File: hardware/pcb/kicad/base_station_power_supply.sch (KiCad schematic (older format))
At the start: 19 parts, among them CON1 CONN_2, IC1 BRIDGE_TART, SW1 SWITCH

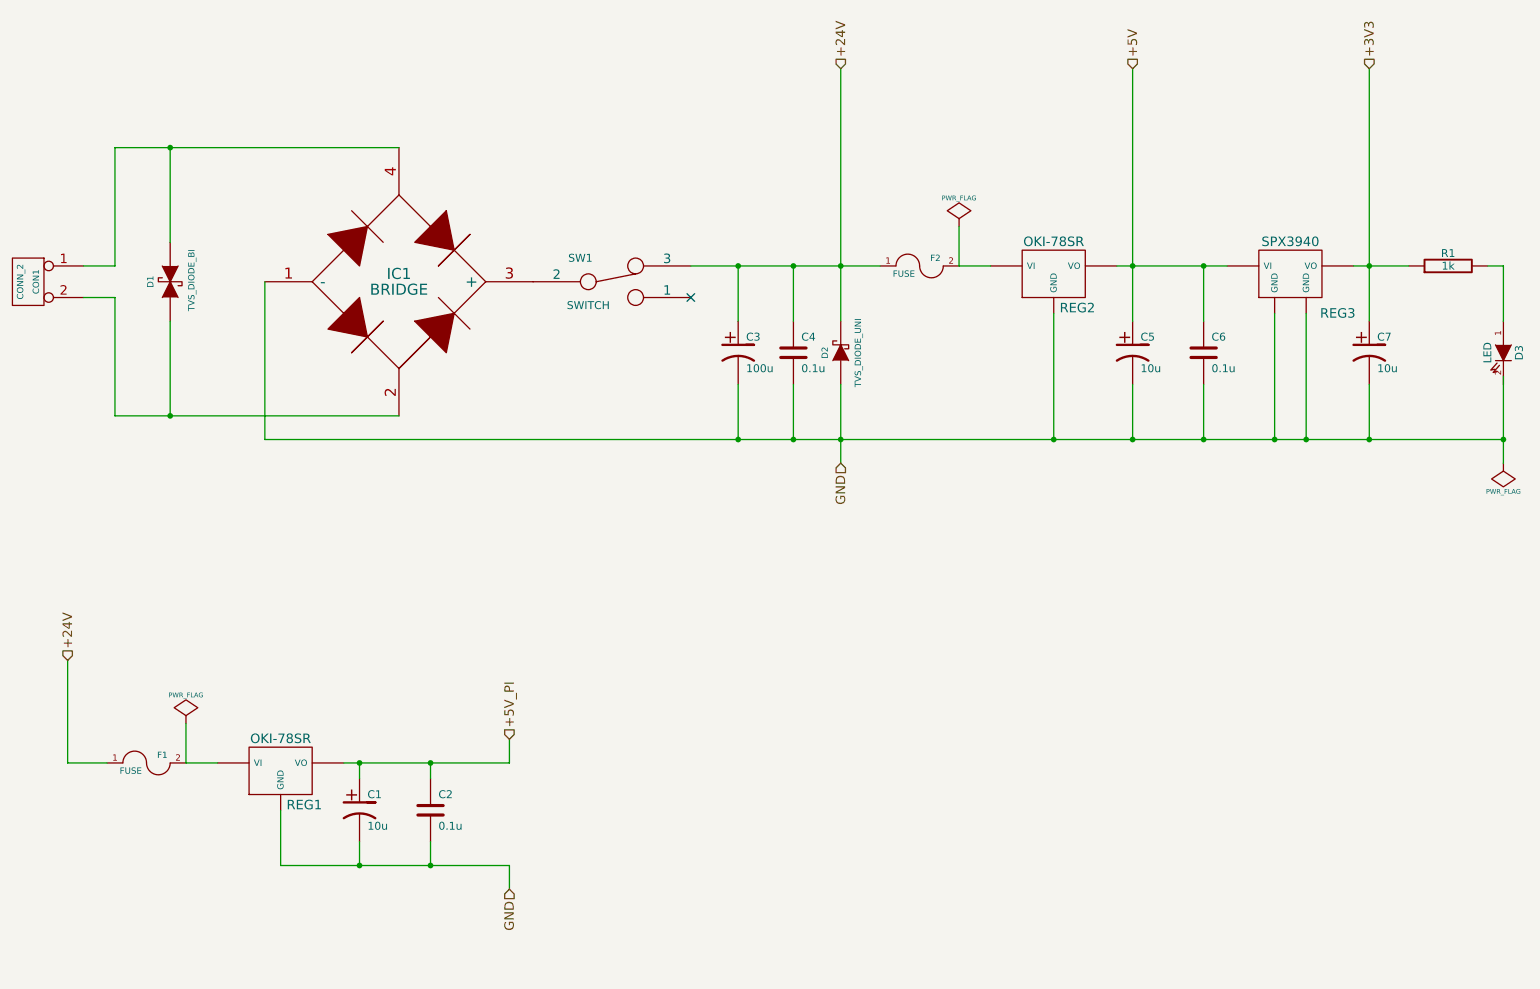
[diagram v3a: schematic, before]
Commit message: Made component references more logical - very similar to eagle version
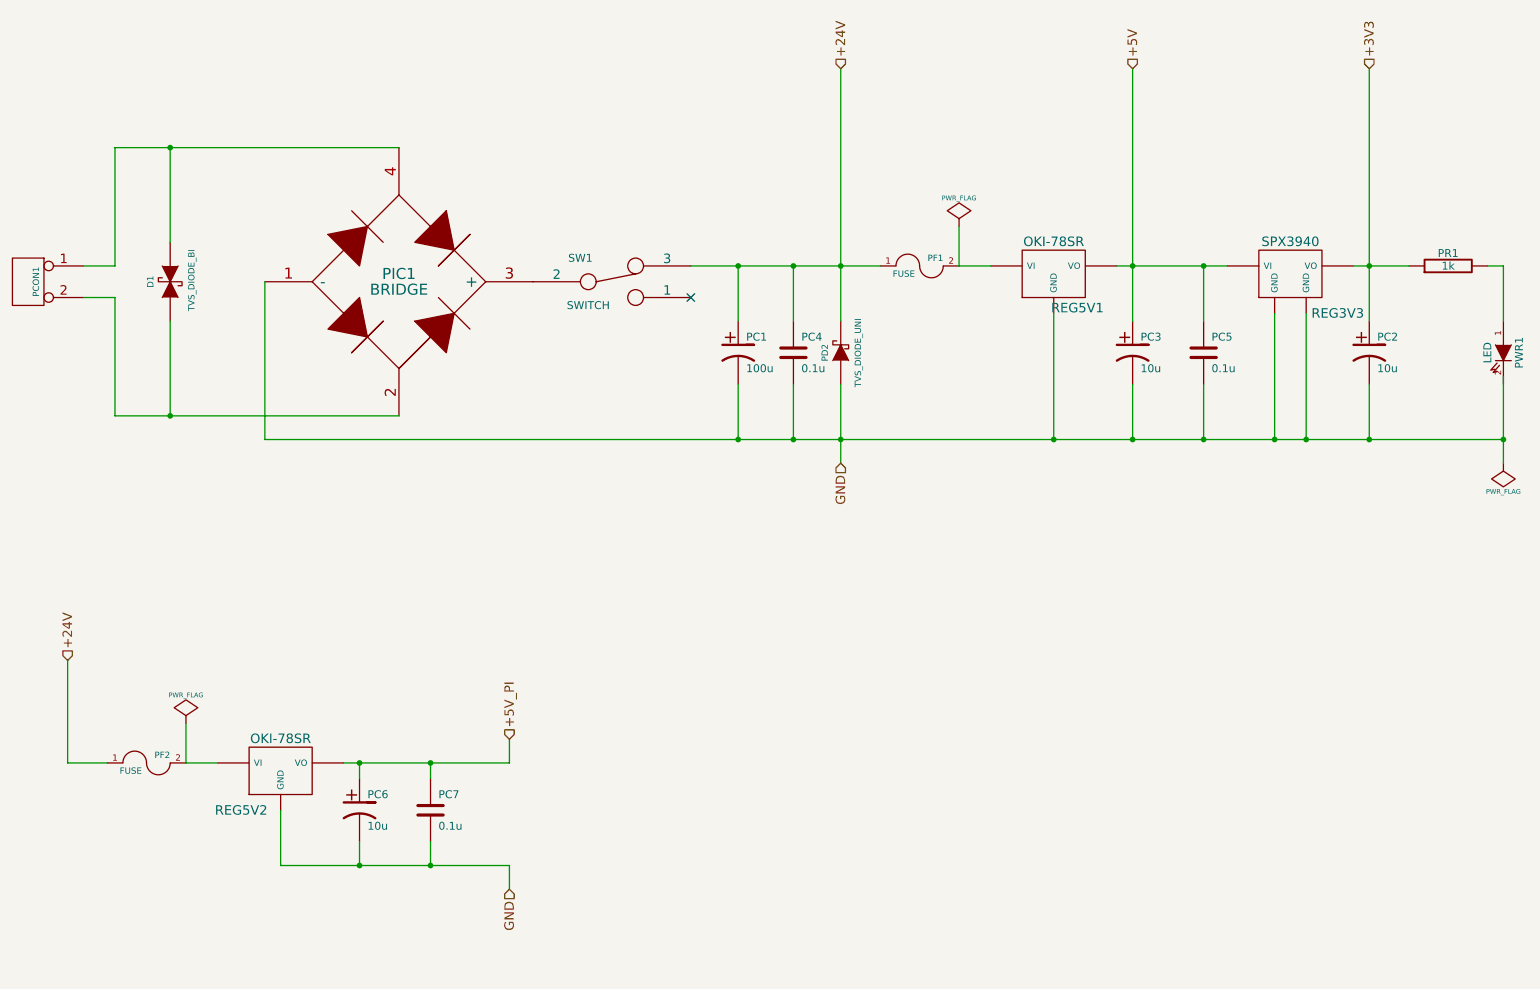
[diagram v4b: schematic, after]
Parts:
- PCON1: renamed from CON1; value CONN_2 -> ~
- renumbered C3 to PC1, C7 to PC2, C5 to PC3, C4 to PC4, C6 to PC5, C1 to PC6, C2 to PC7, D2 to PD2, F2 to PF1, F1 to PF2, IC1 to PIC1, R1 to PR1, D3 to PWR1, REG3 to REG3V3, REG2 to REG5V1, REG1 to REG5V2
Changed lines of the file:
@@
 Sheet 2 7
 Title ""
-Date "4 dec 2014"
+Date "8 dec 2014"
 Rev ""
 Comp ""
@@
 $EndDescr
 $Comp
-L FUSE F1
+L FUSE PF2
 U 1 1 5421F748
 P 1850 5500
-F 0 "F1" H 1950 5550 40  0000 C CNN
+F 0 "PF2" H 1950 5550 40  0000 C CNN
 F 1 "FUSE" H 1750 5450 40  0000 C CNN
 F 2 "" H 1850 5500 60  0001 C CNN
@@
 +5V_PI
 $Comp
-L CP1 C1
+L CP1 PC6
 U 1 1 5421F74A
 P 3200 5800
-F 0 "C1" H 3250 5900 50  0000 L CNN
+F 0 "PC6" H 3250 5900 50  0000 L CNN
 F 1 "10u" H 3250 5700 50  0000 L CNN
 F 2 "E5-10,5_TART" H 3200 5800 60  0001 C CNN
@@
 $EndComp
 $Comp
-L C C2
+L C PC7
 U 1 1 5421F749
 P 3650 5800
-F 0 "C2" H 3700 5900 50  0000 L CNN
+F 0 "PC7" H 3700 5900 50  0000 L CNN
 F 1 "0.1u" H 3700 5700 50  0000 L CNN
 F 2 "" H 3650 5800 60  0001 C CNN
@@
 $EndComp
 $Comp
-L OK1-78SR_TART REG1
+L OK1-78SR_TART REG5V2
 U 1 1 5421F746
 P 2700 5550
-F 0 "REG1" H 2850 5334 60  0000 C CNN
+F 0 "REG5V2" H 2450 5300 60  0000 C CNN
 F 1 "OK1-78SR_TART" H 2700 5860 60  0001 C CNN
 F 2 "" H 2700 5550 60  0001 C CNN
@@
 $EndComp
 $Comp
-L SPX3940_TART REG3
+L SPX3940_TART REG3V3
 U 1 1 5419032C
 P 9100 2400
-F 0 "REG3" H 9400 2150 60  0000 C CNN
+F 0 "REG3V3" H 9400 2150 60  0000 C CNN
 F 1 "SPX3940_TART" H 9100 2710 60  0001 C CNN
 F 2 "" H 9100 2400 60  0001 C CNN
@@
 $EndComp
 $Comp
-L OK1-78SR_TART REG2
+L OK1-78SR_TART REG5V1
 U 1 1 54190317
 P 7600 2400
-F 0 "REG2" H 7750 2184 60  0000 C CNN
+F 0 "REG5V1" H 7750 2184 60  0000 C CNN
 F 1 "OK1-78SR_TART" H 7600 2710 60  0001 C CNN
 F 2 "" H 7600 2400 60  0001 C CNN
@@
 $EndComp
 $Comp
-L TVS_DIODE_UNI_TART D2
+L TVS_DIODE_UNI_TART PD2
 U 1 1 5418D6C0
 P 6250 2900
-F 0 "D2" H 6250 3000 40  0000 C CNN
+F 0 "PD2" H 6250 3000 40  0000 C CNN
 F 1 "TVS_DIODE_UNI_TART" H 6240 3060 40  0001 C CNN
 F 2 "" H 6250 2900 60  0001 C CNN
@@
 $EndComp
 $Comp
-L BRIDGE_TART IC1
+L BRIDGE_TART PIC1
 U 1 1 5418D689
 P 3450 2450
-F 0 "IC1" H 3450 2500 70  0000 C CNN
+F 0 "PIC1" H 3450 2500 70  0000 C CNN
 F 1 "BRIDGE_TART" H 4000 3400 60  0001 C CNN
 F 2 "" H 3450 2450 60  0001 C CNN
@@
 +24V
 $Comp
-L C C4
+L C PC4
 U 1 1 5407CB7A
 P 5950 2900
-F 0 "C4" H 6000 3000 50  0000 L CNN
+F 0 "PC4" H 6000 3000 50  0000 L CNN
 F 1 "0.1u" H 6000 2800 50  0000 L CNN
 F 2 "" H 5950 2900 60  0001 C CNN
@@
 $EndComp
 $Comp
-L CP1 C3
+L CP1 PC1
 U 1 1 5407CB6C
 P 5600 2900
-F 0 "C3" H 5650 3000 50  0000 L CNN
+F 0 "PC1" H 5650 3000 50  0000 L CNN
 F 1 "100u" H 5650 2800 50  0000 L CNN
 F 2 "E5-10,5_TART" H 5600 2900 60  0001 C CNN
@@
 $EndComp
 $Comp
-L FUSE F2
+L FUSE PF1
 U 1 1 5407A432
 P 6750 2350
-F 0 "F2" H 6850 2400 40  0000 C CNN
+F 0 "PF1" H 6850 2400 40  0000 C CNN
 F 1 "FUSE" H 6650 2300 40  0000 C CNN
 F 2 "" H 6750 2350 60  0001 C CNN
@@
 $EndComp
 $Comp
-L LED D3
+L LED PWR1
 U 1 1 5407A3D9
 P 10450 2900
-F 0 "D3" H 10450 3000 50  0000 C CNN
+F 0 "PWR1" H 10450 3000 50  0000 C CNN
 F 1 "LED" H 10450 2800 50  0000 C CNN
 F 2 "" H 10450 2900 60  0001 C CNN
@@
 $EndComp
 $Comp
-L R R1
+L R PR1
 U 1 1 5407A3AD
 P 10100 2350
-F 0 "R1" V 10180 2350 50  0000 C CNN
+F 0 "PR1" V 10180 2350 50  0000 C CNN
 F 1 "1k" V 10100 2350 50  0000 C CNN
 F 2 "" H 10100 2350 60  0001 C CNN
@@
 $EndComp
 $Comp
-L CP1 C7
+L CP1 PC2
 U 1 1 5407A35C
 P 9600 2900
-F 0 "C7" H 9650 3000 50  0000 L CNN
+F 0 "PC2" H 9650 3000 50  0000 L CNN
 F 1 "10u" H 9650 2800 50  0000 L CNN
 F 2 "E2-5_TART" H 9600 2900 60  0001 C CNN
@@
 $EndComp
 $Comp
-L C C6
+L C PC5
 U 1 1 5407A2F7
 P 8550 2900
-F 0 "C6" H 8600 3000 50  0000 L CNN
+F 0 "PC5" H 8600 3000 50  0000 L CNN
 F 1 "0.1u" H 8600 2800 50  0000 L CNN
 F 2 "" H 8550 2900 60  0001 C CNN
@@
 $EndComp
 $Comp
-L CP1 C5
+L CP1 PC3
 U 1 1 5407A2C8
 P 8100 2900
-F 0 "C5" H 8150 3000 50  0000 L CNN
+F 0 "PC3" H 8150 3000 50  0000 L CNN
 F 1 "10u" H 8150 2800 50  0000 L CNN
 F 2 "E5-10,5_TART" H 8100 2900 60  0001 C CNN
@@
 $EndComp
 $Comp
-L CONN_2 CON1
+L CONN_2 PCON1
 U 1 1 542A164F
 P 1100 2450
-F 0 "CON1" V 1050 2450 40  0000 C CNN
-F 1 "CONN_2" V 1150 2450 40  0000 C CNN
+F 0 "PCON1" V 1050 2450 40  0000 C CNN
+F 1 "~" V 1150 2450 40  0000 C CNN
 F 2 "" H 1100 2450 60  0000 C CNN
 F 3 "" H 1100 2450 60  0000 C CNN
